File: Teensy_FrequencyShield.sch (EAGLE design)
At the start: 17 parts, among them IC9 78L05F

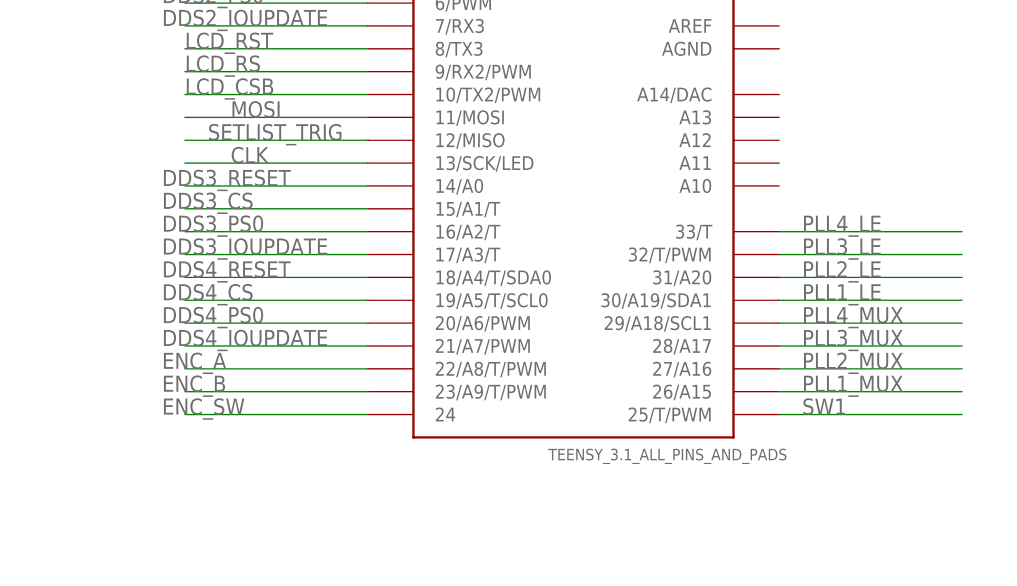
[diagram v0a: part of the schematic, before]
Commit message: Tweaked pin layout; added back in extra DDS & PLL channel names to Teensy pinout
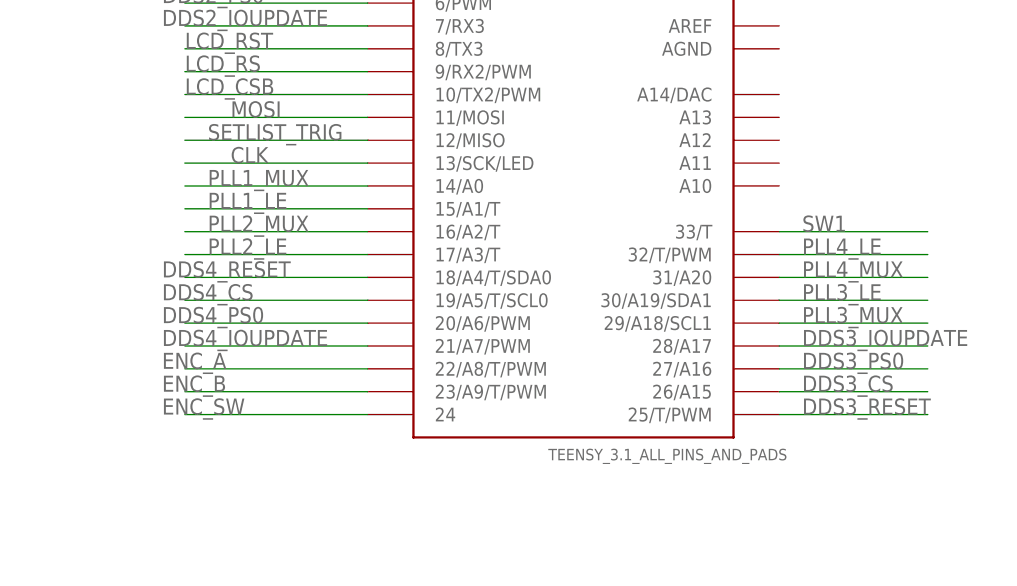
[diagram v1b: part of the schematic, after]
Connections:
- net DDS3_CS: now also TEENSY.26/A15; no longer TEENSY.15/A1/T
- net DDS3_IOUPDATE: now also TEENSY.28/A17; no longer TEENSY.17/A3/T
- net DDS3_PS0: now also TEENSY.27/A16; no longer TEENSY.16/A2/T
- net DDS3_RESET: now also TEENSY.25/T/PWM; no longer TEENSY.14/A0
- net PLL1_LE: now also TEENSY.15/A1/T; no longer TEENSY.30/A19/SDA1
- net PLL1_MUX: now also TEENSY.14/A0; no longer TEENSY.26/A15
- net PLL2_LE: now also TEENSY.17/A3/T; no longer TEENSY.31/A20
- net PLL2_MUX: now also TEENSY.16/A2/T; no longer TEENSY.27/A16
- net PLL3_LE: now also TEENSY.30/A19/SDA1; no longer TEENSY.32/T/PWM
- net PLL3_MUX: now also TEENSY.29/A18/SCL1; no longer TEENSY.28/A17
- net PLL4_LE: now also TEENSY.32/T/PWM; no longer TEENSY.33/T
- net PLL4_MUX: now also TEENSY.31/A20; no longer TEENSY.29/A18/SCL1
- net SW1: now also TEENSY.33/T; no longer TEENSY.25/T/PWM
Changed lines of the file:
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@@
 <?xml version="1.0" encoding="utf-8"?>
 <!DOCTYPE eagle SYSTEM "eagle.dtd">
-<eagle version="6.2">
+<eagle version="6.5.0">
 <drawing>
 <settings>
@@
 <setting verticaltext="up"/>
 </settings>
-<grid distance="0.1" unitdist="inch" unit="inch" style="lines" multiple="1" display="yes" altdistance="0.01" altunitdist="inch" altunit="inch"/>
+<grid distance="0.05" unitdist="inch" unit="inch" style="lines" multiple="1" display="no" altdistance="0.01" altunitdist="inch" altunit="inch"/>
 <layers>
 <layer number="1" name="Top" color="4" fill="1" visible="no" active="no"/>
@@
 </segment>
 <segment>
-<pinref part="TEENSY" gate="G$1" pin="30/A19/SDA1"/>
-<wire x1="93.98" y1="35.56" x2="114.3" y2="35.56" width="0.1524" layer="91"/>
-<label x="96.52" y="35.56" size="1.778" layer="95"/>
+<pinref part="TEENSY" gate="G$1" pin="15/A1/T"/>
+<wire x1="48.26" y1="45.72" x2="27.94" y2="45.72" width="0.1524" layer="91"/>
+<label x="30.48" y="45.72" size="1.778" layer="95"/>
 </segment>
 </net>
@@
 </segment>
 <segment>
-<pinref part="TEENSY" gate="G$1" pin="26/A15"/>
-<wire x1="93.98" y1="25.4" x2="114.3" y2="25.4" width="0.1524" layer="91"/>
-<label x="96.52" y="25.4" size="1.778" layer="95"/>
+<pinref part="TEENSY" gate="G$1" pin="14/A0"/>
+<wire x1="48.26" y1="48.26" x2="27.94" y2="48.26" width="0.1524" layer="91"/>
+<label x="30.48" y="48.26" size="1.778" layer="95"/>
 </segment>
 </net>
@@
 </segment>
 <segment>
-<pinref part="TEENSY" gate="G$1" pin="31/A20"/>
-<wire x1="93.98" y1="38.1" x2="114.3" y2="38.1" width="0.1524" layer="91"/>
-<label x="96.52" y="38.1" size="1.778" layer="95"/>
+<pinref part="TEENSY" gate="G$1" pin="17/A3/T"/>
+<wire x1="48.26" y1="40.64" x2="27.94" y2="40.64" width="0.1524" layer="91"/>
+<label x="30.48" y="40.64" size="1.778" layer="95"/>
 </segment>
 </net>
@@
 </segment>
 <segment>
-<pinref part="TEENSY" gate="G$1" pin="27/A16"/>
-<wire x1="93.98" y1="27.94" x2="114.3" y2="27.94" width="0.1524" layer="91"/>
-<label x="96.52" y="27.94" size="1.778" layer="95"/>
+<pinref part="TEENSY" gate="G$1" pin="16/A2/T"/>
+<wire x1="48.26" y1="43.18" x2="27.94" y2="43.18" width="0.1524" layer="91"/>
+<label x="30.48" y="43.18" size="1.778" layer="95"/>
 </segment>
 </net>
@@
 </segment>
 <segment>
-<pinref part="TEENSY" gate="G$1" pin="32/T/PWM"/>
-<wire x1="93.98" y1="40.64" x2="114.3" y2="40.64" width="0.1524" layer="91"/>
-<label x="96.52" y="40.64" size="1.778" layer="95"/>
+<pinref part="TEENSY" gate="G$1" pin="30/A19/SDA1"/>
+<wire x1="93.98" y1="35.56" x2="110.49" y2="35.56" width="0.1524" layer="91"/>
+<label x="96.52" y="35.56" size="1.778" layer="95"/>
 </segment>
 </net>
@@
 </segment>
 <segment>
-<pinref part="TEENSY" gate="G$1" pin="28/A17"/>
-<wire x1="93.98" y1="30.48" x2="114.3" y2="30.48" width="0.1524" layer="91"/>
-<label x="96.52" y="30.48" size="1.778" layer="95"/>
+<pinref part="TEENSY" gate="G$1" pin="29/A18/SCL1"/>
+<wire x1="93.98" y1="33.02" x2="110.49" y2="33.02" width="0.1524" layer="91"/>
+<label x="96.52" y="33.02" size="1.778" layer="95"/>
 </segment>
 </net>
@@
 </segment>
 <segment>
-<pinref part="TEENSY" gate="G$1" pin="33/T"/>
-<wire x1="93.98" y1="43.18" x2="114.3" y2="43.18" width="0.1524" layer="91"/>
-<label x="96.52" y="43.18" size="1.778" layer="95"/>
+<pinref part="TEENSY" gate="G$1" pin="32/T/PWM"/>
+<wire x1="93.98" y1="40.64" x2="110.49" y2="40.64" width="0.1524" layer="91"/>
+<label x="96.52" y="40.64" size="1.778" layer="95"/>
 </segment>
 </net>
@@
 </segment>
 <segment>
-<pinref part="TEENSY" gate="G$1" pin="29/A18/SCL1"/>
-<wire x1="93.98" y1="33.02" x2="114.3" y2="33.02" width="0.1524" layer="91"/>
-<label x="96.52" y="33.02" size="1.778" layer="95"/>
+<pinref part="TEENSY" gate="G$1" pin="31/A20"/>
+<wire x1="93.98" y1="38.1" x2="110.49" y2="38.1" width="0.1524" layer="91"/>
+<label x="96.52" y="38.1" size="1.778" layer="95"/>
 </segment>
 </net>
@@
 </segment>
 <segment>
-<pinref part="TEENSY" gate="G$1" pin="14/A0"/>
-<wire x1="48.26" y1="48.26" x2="27.94" y2="48.26" width="0.1524" layer="91"/>
-<label x="25.4" y="48.26" size="1.778" layer="95"/>
+<pinref part="TEENSY" gate="G$1" pin="25/T/PWM"/>
+<wire x1="93.98" y1="22.86" x2="110.49" y2="22.86" width="0.1524" layer="91"/>
+<label x="96.52" y="22.86" size="1.778" layer="95"/>
 </segment>
 </net>
@@
 </segment>
 <segment>
-<pinref part="TEENSY" gate="G$1" pin="15/A1/T"/>
-<wire x1="48.26" y1="45.72" x2="27.94" y2="45.72" width="0.1524" layer="91"/>
-<label x="25.4" y="45.72" size="1.778" layer="95"/>
+<pinref part="TEENSY" gate="G$1" pin="26/A15"/>
+<wire x1="93.98" y1="25.4" x2="110.49" y2="25.4" width="0.1524" layer="91"/>
+<label x="96.52" y="25.4" size="1.778" layer="95"/>
 </segment>
 </net>
@@
 </segment>
 <segment>
-<pinref part="TEENSY" gate="G$1" pin="16/A2/T"/>
-<wire x1="48.26" y1="43.18" x2="27.94" y2="43.18" width="0.1524" layer="91"/>
-<label x="25.4" y="43.18" size="1.778" layer="95"/>
+<pinref part="TEENSY" gate="G$1" pin="27/A16"/>
+<wire x1="93.98" y1="27.94" x2="110.49" y2="27.94" width="0.1524" layer="91"/>
+<label x="96.52" y="27.94" size="1.778" layer="95"/>
 </segment>
 </net>
@@
 </segment>
 <segment>
-<pinref part="TEENSY" gate="G$1" pin="17/A3/T"/>
-<wire x1="48.26" y1="40.64" x2="27.94" y2="40.64" width="0.1524" layer="91"/>
-<label x="25.4" y="40.64" size="1.778" layer="95"/>
+<pinref part="TEENSY" gate="G$1" pin="28/A17"/>
+<wire x1="93.98" y1="30.48" x2="110.49" y2="30.48" width="0.1524" layer="91"/>
+<label x="96.52" y="30.48" size="1.778" layer="95"/>
 </segment>
 </net>
@@
 </segment>
 <segment>
-<pinref part="TEENSY" gate="G$1" pin="25/T/PWM"/>
-<wire x1="93.98" y1="22.86" x2="114.3" y2="22.86" width="0.1524" layer="91"/>
-<label x="96.52" y="22.86" size="1.778" layer="95"/>
-</segment>
-</net>
+<pinref part="TEENSY" gate="G$1" pin="33/T"/>
+<wire x1="93.98" y1="43.18" x2="110.49" y2="43.18" width="0.1524" layer="91"/>
+<label x="96.52" y="43.18" size="1.778" layer="95"/>
+</segment>
+</net>

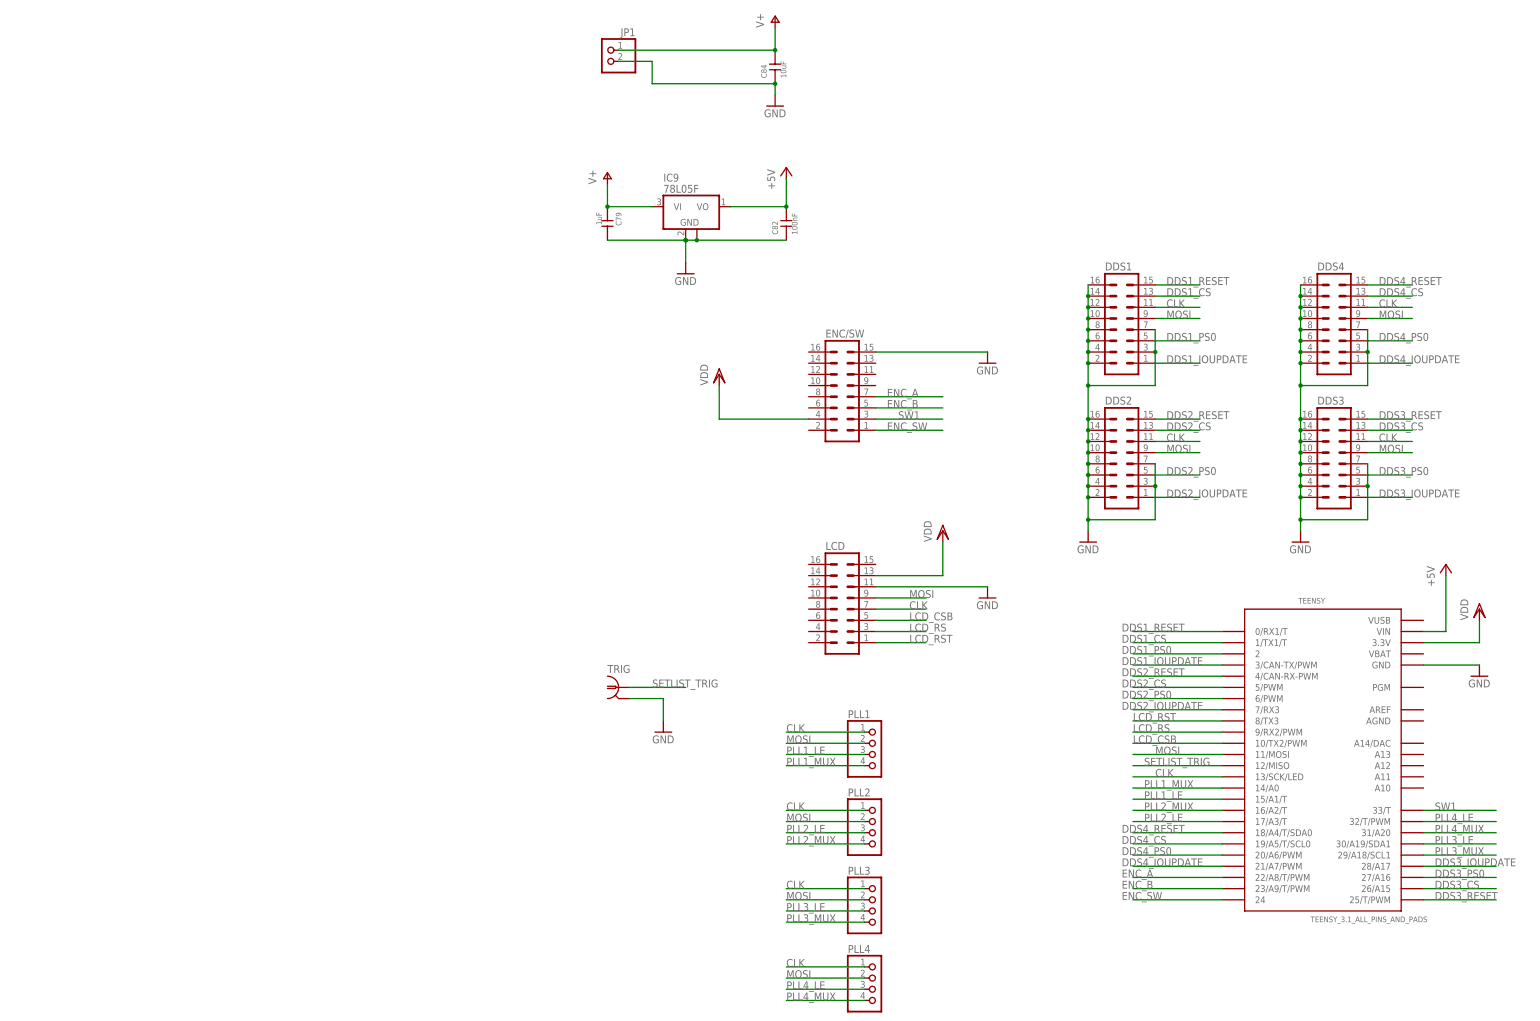
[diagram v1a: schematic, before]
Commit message: Routed generic frequency breakout shield for teensy
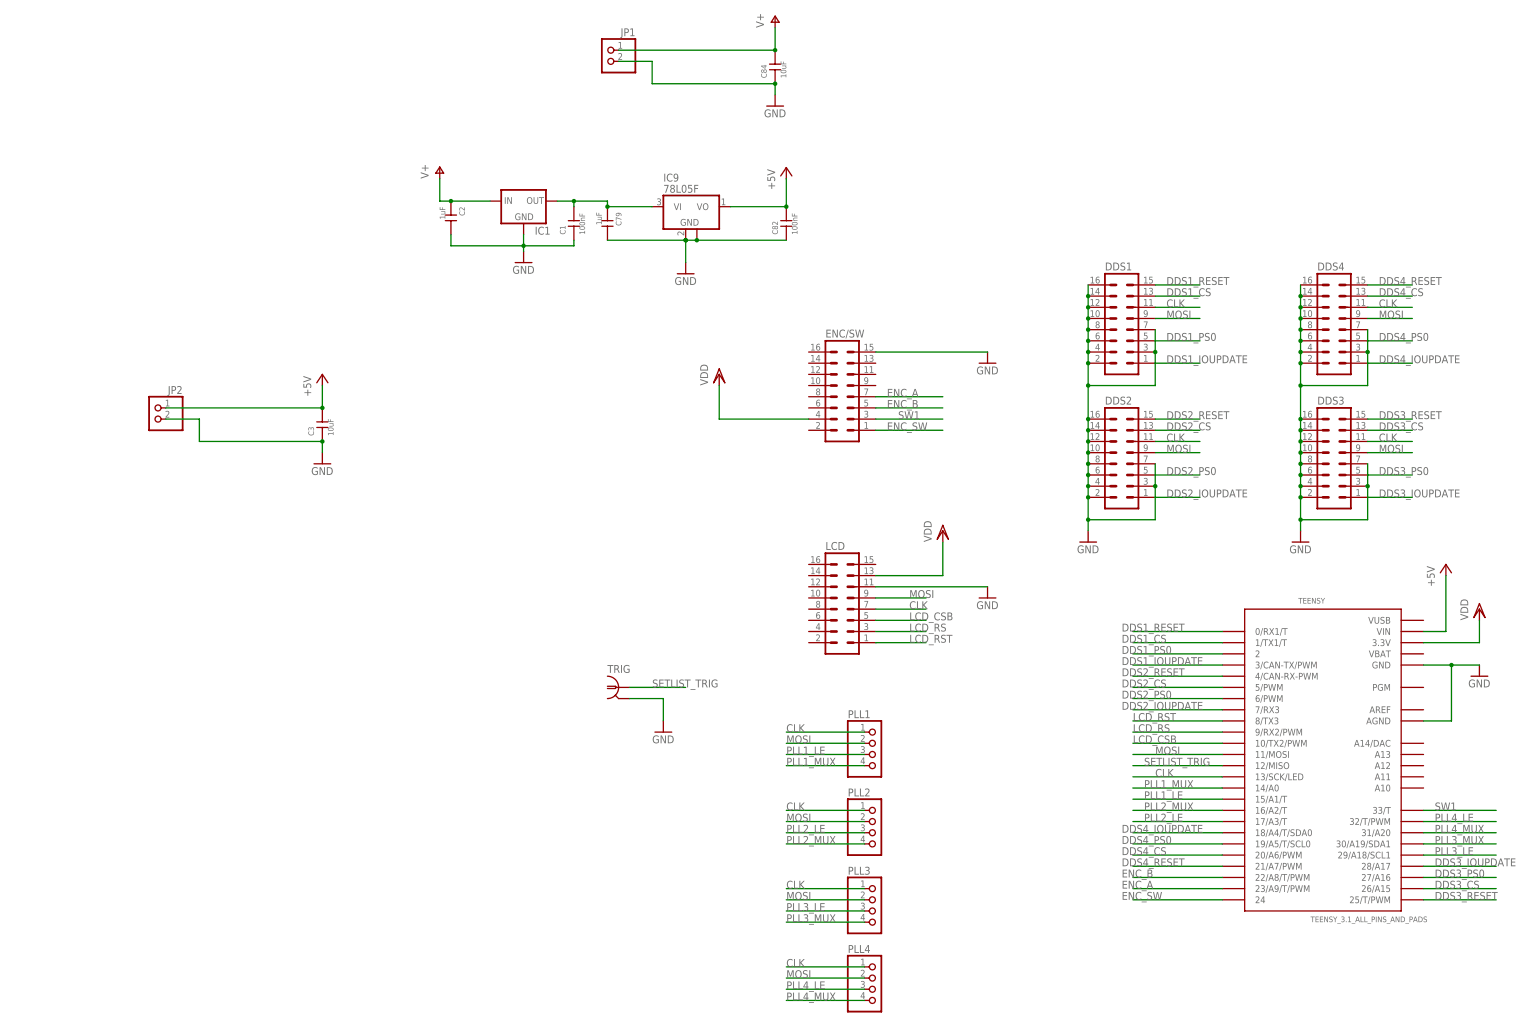
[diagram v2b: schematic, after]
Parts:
- added C1: 100nF, rlc-jqi:CAP0603
- added C2: 1uF, rlc-jqi:CAP0805
- added C3: 10uF, rlc-jqi:CAP0805
- added IC1: (no value), regulator-jqi:78XX-TO220
- added JP2: (no value), pinhead:PINHD-1X2
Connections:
- new net N$2: C1.P$2, C79.P$1, IC1.OUT, IC9.VI
- net +5V: now also C3.P$2, JP2.1
- net DDS4_CS: now also TEENSY.20/A6/PWM; no longer TEENSY.19/A5/T/SCL0
- net DDS4_IOUPDATE: now also TEENSY.18/A4/T/SDA0; no longer TEENSY.21/A7/PWM
- net DDS4_PS0: now also TEENSY.19/A5/T/SCL0; no longer TEENSY.20/A6/PWM
- net DDS4_RESET: now also TEENSY.21/A7/PWM; no longer TEENSY.18/A4/T/SDA0
- net ENC_A: now also TEENSY.23/A9/T/PWM; no longer TEENSY.22/A8/T/PWM
- net ENC_B: now also TEENSY.22/A8/T/PWM; no longer TEENSY.23/A9/T/PWM
- net GND: now also C1.P$1, C2.P$2, C3.P$1, IC1.GND, JP2.2, TEENSY.AGND
- net PLL3_LE: now also TEENSY.29/A18/SCL1; no longer TEENSY.30/A19/SDA1
- net PLL3_MUX: now also TEENSY.30/A19/SDA1; no longer TEENSY.29/A18/SCL1
- net V+: now also C2.P$1, IC1.IN; no longer C79.P$1, IC9.VI

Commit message: Added optional adjustable Vreg, in case need other voltage.
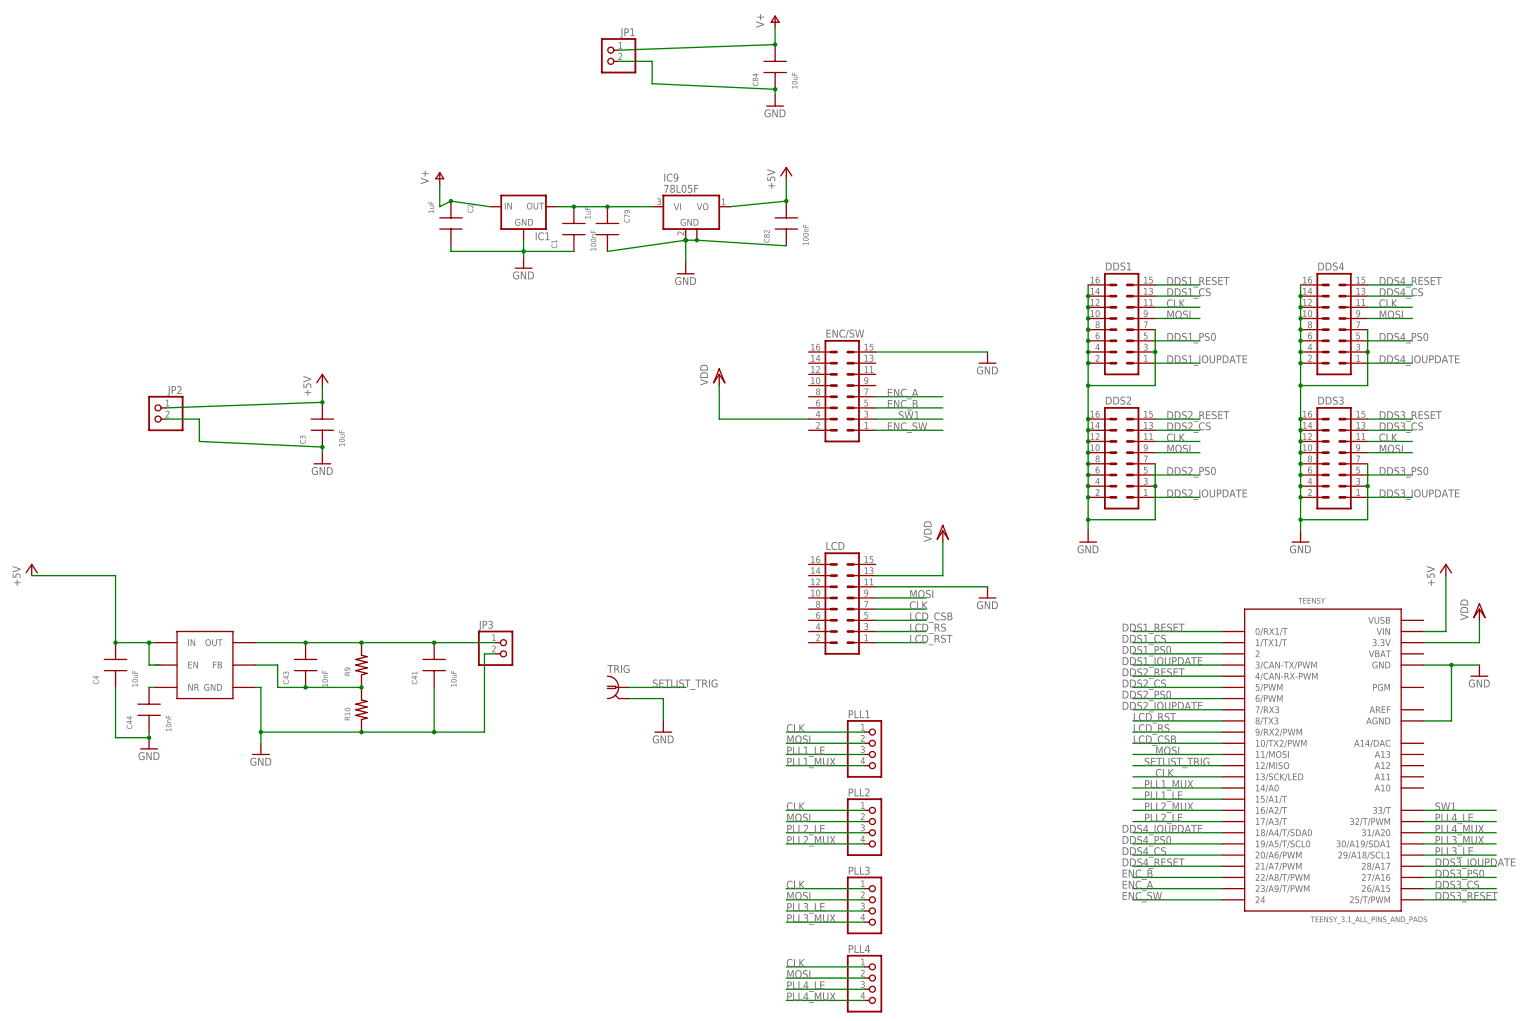
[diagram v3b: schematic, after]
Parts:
- added C4, C41: 10uF, rlc-jqi:CAP0805
- added C43, C44: 10nF, rlc-jqi:CAP0603
- added JP3: (no value), pinhead:PINHD-1X2
- added R10, R9: (no value), rlc-jqi:RES0603
- added U4: TPS7A4901, aom_driver:TPS7A49XX
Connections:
- new net N$1: C41.P$2, C43.P$2, JP3.1, R9.P$2, U4.OUT
- new net N$49: C43.P$1, R10.P$2, R9.P$1, U4.FB
- new net N$51: C44.P$2, U4.NR
- net +5V: now also C4.P$2, U4.IN
- net GND: now also C4.P$1, C41.P$1, C44.P$1, JP3.2, R10.P$1, U4.GND
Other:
- moved on the sheet: C1, C2, C79, IC1
